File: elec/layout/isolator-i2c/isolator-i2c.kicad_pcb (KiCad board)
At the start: 2 copper layers, 7 parts, among them U1 10kΩ ±1% 62.5mW, U2 10kΩ ±1% 62.5mW, U4 10kΩ ±1% 62.5mW, U5 10kΩ ±1% 62.5mW, U6 100nF ±10% 16V X7R, U7 100nF ±10% 16V X7R

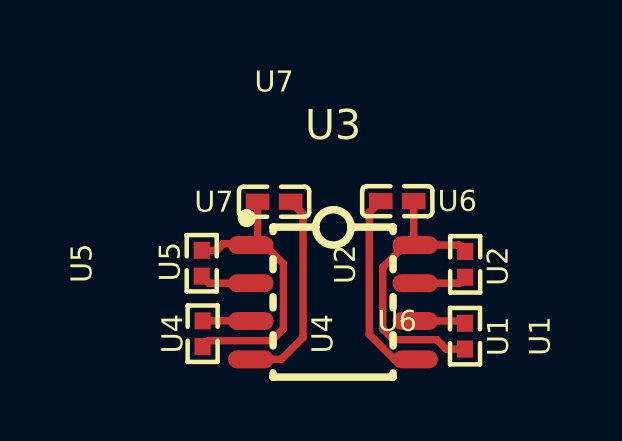
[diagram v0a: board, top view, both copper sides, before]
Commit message: update layouts to kicad 9
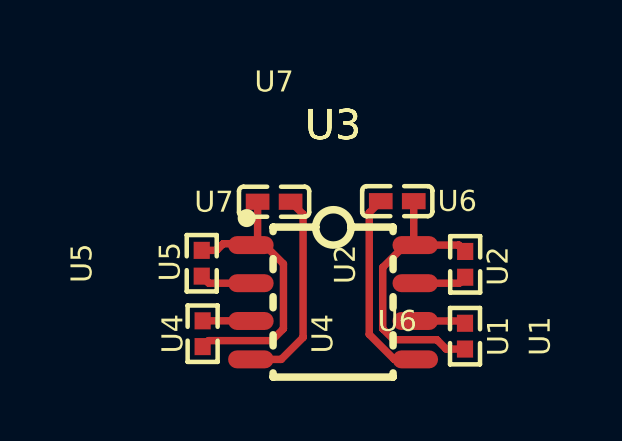
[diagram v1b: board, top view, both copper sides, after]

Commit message: update LED gpio pin
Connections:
- U3 pad 2: line-3 -> line-1
- U3 pad 3: line-1 -> line-3
- U3 pad 4: gnd -> gnd-1
- U3 pad 5: gnd-1 -> gnd
- U4 pad 1: line-1 -> line-3
- U5 pad 1: line-3 -> line-1
- U6 pad 2: gnd-1 -> gnd
- U7 pad 2: gnd -> gnd-1

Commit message: restore layout files
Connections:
- U3 pad 2: line-1 -> line-3
- U3 pad 3: line-3 -> line-1
- U3 pad 4: gnd-1 -> gnd
- U3 pad 5: gnd -> gnd-1
- U4 pad 1: line-3 -> line-1
- U5 pad 1: line-1 -> line-3
- U6 pad 2: gnd -> gnd-1
- U7 pad 2: gnd-1 -> gnd

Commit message: building frozen
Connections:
- U1 pad 1: line-2 -> line-1
- U1 pad 2: hv-1 -> hv
- U2 pad 1: line -> line-2
- U2 pad 2: hv-1 -> hv
- U3 pad 1: hv -> hv-1
- U3 pad 2: line-3 -> line
- U3 pad 3: line-1 -> line-3
- U3 pad 6: line-2 -> line-1
- U3 pad 7: line -> line-2
- U3 pad 8: hv-1 -> hv
- U4 pad 1: line-1 -> line-3
- U4 pad 2: hv -> hv-1
- U5 pad 1: line-3 -> line
- U5 pad 2: hv -> hv-1
- U6 pad 1: hv-1 -> hv
- U7 pad 1: hv -> hv-1

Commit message: building locally to fix frozen builds
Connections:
- U1 pad 1: line-1 -> line-2
- U2 pad 1: line-2 -> line-3
- U3 pad 3: line-3 -> line-1
- U3 pad 4: gnd -> gnd-1
- U3 pad 5: gnd-1 -> gnd
- U3 pad 6: line-1 -> line-2
- U3 pad 7: line-2 -> line-3
- U4 pad 1: line-3 -> line-1
- U6 pad 2: gnd-1 -> gnd
- U7 pad 2: gnd -> gnd-1
